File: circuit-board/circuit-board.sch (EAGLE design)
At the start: 42 parts, among them IC1 UA78M05DCY, Q1 BC547B, U1 MAX3232, U2 ATMEGA328P_TQFP, U3 ADUM1201BRZ, Y1 16MHz

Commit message: Delete V1 circuit board, replace with V2 working file
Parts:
- removed Y1: 16MHz, SparkFun-Clocks:CRYSTAL-16MHZPTH-HC49US
- added C1, C2, C21: 10uF, adafruit:CPOL-USE2.5-5
- added MIC-XFMR, SPK-XFMR: 42TL016, trafo-xicon:42TL016
- added OK1: 4N25SM, optocoupler:4N25SM
- added Q2: BC547B, transistor-npn:BC547B
- added R8: TRIMPOT, SparkFun:TRIMPOT
- added R9: (no value), rcl-2:R-TRIMM3296W
- added Y2: 16MHz, SparkFun-Clocks:CRYSTAL-GROUNDEDSMD-3.2X2.5
- R2: value 10k -> 120; device resistor:R-TRIMMT93YA -> SparkFun-Resistors:RESISTOR0603
- R6: value 0 -> 220; device SparkFun-Resistors:0OHM-0603-1/10W-5% -> SparkFun-Resistors:220OHM-0603-1/10W-1%
- renumbered 12V-IN to 12V-IN-GPS
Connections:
- new net N$2: C2.-, SPK-XFMR.6
- new net N$5: C2.+, Q2.B, R9.A
- new net N$6: C21.-, SPK-XFMR.1
- new net N$7: C5.-, MIC-XFMR.6
- new net N$9: OK1.A, R6.1
- new net RADIO-PTT-SENSE: OK1.COL, R4.2
- new net SPKAMP: C1.+, Q2.C, R2.1, R9.S
- net 12V: now also R2.2, R6.2
- net GND: now also MIC-XFMR.4, OK1.EMI, SPK-XFMR.3
- net GNDA: now also MIC-XFMR.3, Q2.E, SPK-XFMR.4, Y2.3
- net HANDSET-MIC: now also MIC-XFMR.1; no longer C5.-
- net HANDSET-PTT: now also OK1.C; no longer R4.1
- net HANDSET-SPK: now also C1.-; no longer R6.1
- net N$23: now also Y2.2; no longer Y1.2
- net N$24: now also Y2.1; no longer Y1.1
- net N$3: now also R8.CW; no longer R2.S
- net N$4: now also R8.WIPER; no longer R2.E
- net RADIO-MIC/PTT: now also R4.1; no longer R4.2
- net RADIO-SPK-OUT: now also C21.+; no longer R6.2
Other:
- moved on the sheet: C16, C17, C18, C19, C20, C5, C9, FB1, IC1, Q1, R3, R4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

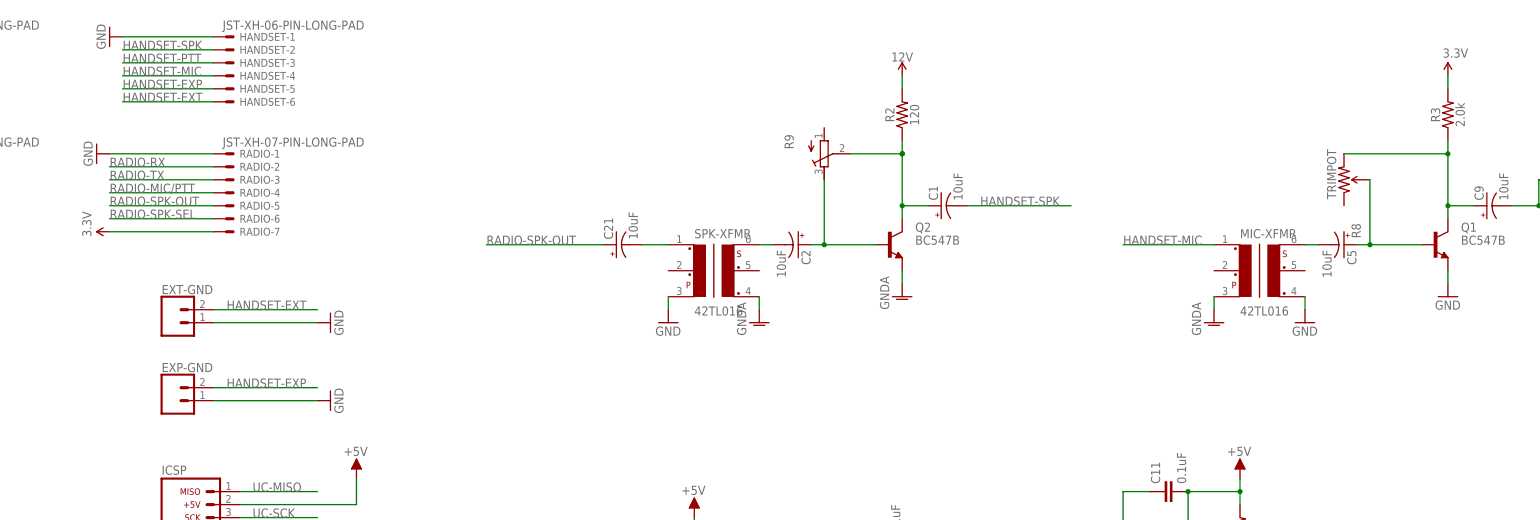
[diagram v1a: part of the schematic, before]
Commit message: Start new circuit board, fix some small circuit design issues
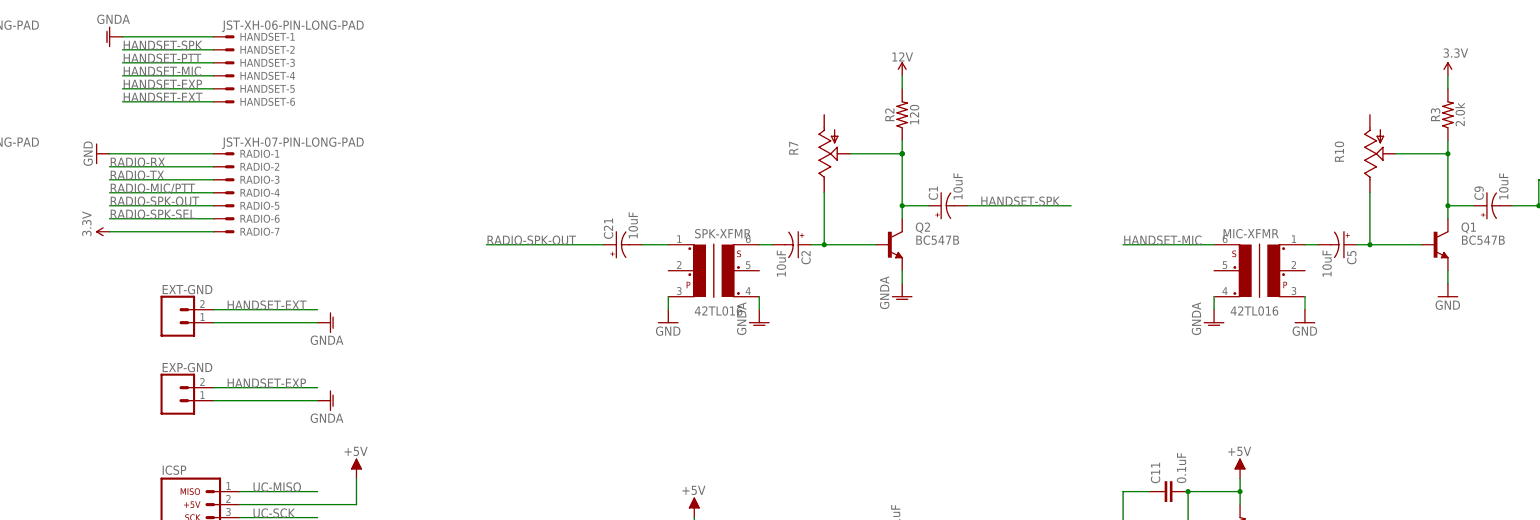
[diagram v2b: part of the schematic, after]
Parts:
- removed R8: TRIMPOT, SparkFun:TRIMPOT
- removed R9: (no value), rcl-2:R-TRIMM3296W
- added R10, R7: (no value), pot:TRIM_US-S64W
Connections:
- net GND: now also MIC-XFMR.3; no longer EXP-GND.1, EXT-GND.1, HANDSET-1.S, MIC-XFMR.4
- net GNDA: now also EXP-GND.1, EXT-GND.1, HANDSET-1.S, MIC-XFMR.4; no longer MIC-XFMR.3
- net HANDSET-MIC: now also MIC-XFMR.6; no longer MIC-XFMR.1
- net N$3: now also R10.S; no longer R8.CW
- net N$4: now also R10.E; no longer R8.WIPER
- net N$5: now also R7.E; no longer R9.A
- net N$7: now also MIC-XFMR.1; no longer MIC-XFMR.6
- net SPKAMP: now also R7.S; no longer R9.S

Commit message: Lay out circuit board, preliminary
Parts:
- renumbered 12V-IN-GPS to 12V-IN
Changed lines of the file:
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@@
 </classes>
 <parts>
-<part name="12V-IN-GPS" library="Rembrandt Electronics - JST XH Connectors v1-0" deviceset="JST-XH-02-PIN" device="-LONG-PAD"/>
+<part name="12V-IN" library="Rembrandt Electronics - JST XH Connectors v1-0" deviceset="JST-XH-02-PIN" device="-LONG-PAD"/>
 <part name="HANDSET" library="Rembrandt Electronics - JST XH Connectors v1-0" deviceset="JST-XH-06-PIN" device="-LONG-PAD"/>
 <part name="SUPPLY2" library="SparkFun-PowerSymbols" deviceset="12V" device=""/>
@@
 </plain>
 <instances>
-<instance part="12V-IN-GPS" gate="-2" x="-261.62" y="241.3"/>
-<instance part="12V-IN-GPS" gate="-1" x="-261.62" y="243.84"/>
+<instance part="12V-IN" gate="-2" x="-261.62" y="241.3"/>
+<instance part="12V-IN" gate="-1" x="-261.62" y="243.84"/>
 <instance part="HANDSET" gate="-1" x="-198.12" y="243.84"/>
 <instance part="HANDSET" gate="-2" x="-198.12" y="241.3"/>
@@
 </segment>
 <segment>
-<pinref part="12V-IN-GPS" gate="-1" pin="S"/>
+<pinref part="12V-IN" gate="-1" pin="S"/>
 <wire x1="-264.16" y1="243.84" x2="-269.24" y2="243.84" width="0.1524" layer="91"/>
 <pinref part="GND5" gate="1" pin="GNDA"/>
@@
 <segment>
 <pinref part="SUPPLY2" gate="G$1" pin="12V"/>
-<pinref part="12V-IN-GPS" gate="-2" pin="S"/>
+<pinref part="12V-IN" gate="-2" pin="S"/>
 <wire x1="-269.24" y1="241.3" x2="-264.16" y2="241.3" width="0.1524" layer="91"/>
 </segment>

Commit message: Add ground planes, routes to V2 board
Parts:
- R10, R7: value (none) -> 100k
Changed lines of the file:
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@@
 <grid distance="0.1" unitdist="inch" unit="inch" style="lines" multiple="1" display="no" altdistance="0.01" altunitdist="inch" altunit="inch"/>
 <layers>
-<layer number="1" name="Top" color="4" fill="1" visible="no" active="no"/>
-<layer number="16" name="Bottom" color="1" fill="1" visible="no" active="no"/>
-<layer number="17" name="Pads" color="2" fill="1" visible="no" active="no"/>
-<layer number="18" name="Vias" color="2" fill="1" visible="no" active="no"/>
-<layer number="19" name="Unrouted" color="6" fill="1" visible="no" active="no"/>
-<layer number="20" name="Dimension" color="15" fill="1" visible="no" active="no"/>
-<layer number="21" name="tPlace" color="7" fill="1" visible="no" active="no"/>
-<layer number="22" name="bPlace" color="7" fill="1" visible="no" active="no"/>
-<layer number="23" name="tOrigins" color="15" fill="1" visible="no" active="no"/>
-<layer number="24" name="bOrigins" color="15" fill="1" visible="no" active="no"/>
-<layer number="25" name="tNames" color="7" fill="1" visible="no" active="no"/>
-<layer number="26" name="bNames" color="7" fill="1" visible="no" active="no"/>
-<layer number="27" name="tValues" color="7" fill="1" visible="no" active="no"/>
-<layer number="28" name="bValues" color="7" fill="1" visible="no" active="no"/>
+<layer number="1" name="Top" color="4" fill="1" visible="yes" active="no"/>
+<layer number="16" name="Bottom" color="1" fill="1" visible="yes" active="no"/>
+<layer number="17" name="Pads" color="2" fill="1" visible="yes" active="no"/>
+<layer number="18" name="Vias" color="2" fill="1" visible="yes" active="no"/>
+<layer number="19" name="Unrouted" color="6" fill="1" visible="yes" active="no"/>
+<layer number="20" name="Dimension" color="24" fill="1" visible="yes" active="no"/>
+<layer number="21" name="tPlace" color="7" fill="1" visible="yes" active="no"/>
+<layer number="22" name="bPlace" color="7" fill="1" visible="yes" active="no"/>
+<layer number="23" name="tOrigins" color="15" fill="1" visible="yes" active="no"/>
+<layer number="24" name="bOrigins" color="15" fill="1" visible="yes" active="no"/>
+<layer number="25" name="tNames" color="7" fill="1" visible="yes" active="no"/>
+<layer number="26" name="bNames" color="7" fill="1" visible="yes" active="no"/>
+<layer number="27" name="tValues" color="7" fill="1" visible="yes" active="no"/>
+<layer number="28" name="bValues" color="7" fill="1" visible="yes" active="no"/>
 <layer number="29" name="tStop" color="7" fill="3" visible="no" active="no"/>
 <layer number="30" name="bStop" color="7" fill="6" visible="no" active="no"/>
@@
 <layer number="35" name="tGlue" color="7" fill="4" visible="no" active="no"/>
 <layer number="36" name="bGlue" color="7" fill="5" visible="no" active="no"/>
-<layer number="37" name="tTest" color="7" fill="1" visible="no" active="no"/>
-<layer number="38" name="bTest" color="7" fill="1" visible="no" active="no"/>
+<layer number="37" name="tTest" color="7" fill="1" visible="yes" active="no"/>
+<layer number="38" name="bTest" color="7" fill="1" visible="yes" active="no"/>
 <layer number="39" name="tKeepout" color="4" fill="11" visible="no" active="no"/>
 <layer number="40" name="bKeepout" color="1" fill="11" visible="no" active="no"/>
@@
 <layer number="44" name="Drills" color="7" fill="1" visible="no" active="no"/>
 <layer number="45" name="Holes" color="7" fill="1" visible="no" active="no"/>
-<layer number="46" name="Milling" color="3" fill="1" visible="no" active="no"/>
-<layer number="47" name="Measures" color="7" fill="1" visible="no" active="no"/>
-<layer number="48" name="Document" color="7" fill="1" visible="no" active="no"/>
-<layer number="49" name="Reference" color="7" fill="1" visible="no" active="no"/>
-<layer number="50" name="dxf" color="7" fill="1" visible="no" active="no"/>
-<layer number="51" name="tDocu" color="7" fill="1" visible="no" active="no"/>
-<layer number="52" name="bDocu" color="7" fill="1" visible="no" active="no"/>
-<layer number="53" name="tGND_GNDA" color="7" fill="9" visible="no" active="no"/>
-<layer number="54" name="bGND_GNDA" color="1" fill="9" visible="no" active="no"/>
-<layer number="56" name="wert" color="7" fill="1" visible="no" active="no"/>
-<layer number="57" name="tCAD" color="7" fill="1" visible="no" active="no"/>
-<layer number="59" name="tCarbon" color="7" fill="1" visible="no" active="no"/>
-<layer number="60" name="bCarbon" color="7" fill="1" visible="no" active="no"/>
+<layer number="46" name="Milling" color="3" fill="1" visible="yes" active="no"/>
+<layer number="47" name="Measures" color="7" fill="1" visible="yes" active="no"/>
+<layer number="48" name="Document" color="7" fill="1" visible="yes" active="no"/>
+<layer number="49" name="Reference" color="7" fill="1" visible="yes" active="no"/>
+<layer number="50" name="dxf" color="7" fill="1" visible="yes" active="no"/>
+<layer number="51" name="tDocu" color="7" fill="1" visible="yes" active="no"/>
+<layer number="52" name="bDocu" color="7" fill="1" visible="yes" active="no"/>
+<layer number="53" name="tGND_GNDA" color="7" fill="9" visible="yes" active="no"/>
+<layer number="54" name="bGND_GNDA" color="1" fill="9" visible="yes" active="no"/>
+<layer number="56" name="wert" color="7" fill="1" visible="yes" active="no"/>
+<layer number="57" name="tCAD" color="7" fill="1" visible="yes" active="no"/>
+<layer number="59" name="tCarbon" color="7" fill="1" visible="yes" active="no"/>
+<layer number="60" name="bCarbon" color="7" fill="1" visible="yes" active="no"/>
 <layer number="88" name="SimResults" color="9" fill="1" visible="yes" active="yes"/>
 <layer number="89" name="SimProbes" color="9" fill="1" visible="yes" active="yes"/>
@@
 <part name="GND24" library="supply1" deviceset="GNDA" device=""/>
 <part name="MIC-XFMR" library="trafo-xicon" library_urn="urn:adsk.eagle:library:393" deviceset="42T?*" device="L" package3d_urn="urn:adsk.eagle:package:28185/1" technology="016"/>
-<part name="R10" library="pot" library_urn="urn:adsk.eagle:library:331" deviceset="TRIM_US-" device="S64W" package3d_urn="urn:adsk.eagle:package:22708/1"/>
-<part name="R7" library="pot" library_urn="urn:adsk.eagle:library:331" deviceset="TRIM_US-" device="S64W" package3d_urn="urn:adsk.eagle:package:22708/1"/>
+<part name="R10" library="pot" library_urn="urn:adsk.eagle:library:331" deviceset="TRIM_US-" device="S64W" package3d_urn="urn:adsk.eagle:package:22708/1" value="100k"/>
+<part name="R7" library="pot" library_urn="urn:adsk.eagle:library:331" deviceset="TRIM_US-" device="S64W" package3d_urn="urn:adsk.eagle:package:22708/1" value="100k"/>
 <part name="GND10" library="supply1" deviceset="GNDA" device=""/>
 <part name="GND11" library="supply1" deviceset="GNDA" device=""/>

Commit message: Route V2 board manually, fix up silkscreen
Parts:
- U2: value ATMEGA328P_TQFP -> ATMEGA328P
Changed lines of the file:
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@@
 <grid distance="0.1" unitdist="inch" unit="inch" style="lines" multiple="1" display="no" altdistance="0.01" altunitdist="inch" altunit="inch"/>
 <layers>
-<layer number="1" name="Top" color="4" fill="1" visible="yes" active="no"/>
-<layer number="16" name="Bottom" color="1" fill="1" visible="yes" active="no"/>
-<layer number="17" name="Pads" color="2" fill="1" visible="yes" active="no"/>
-<layer number="18" name="Vias" color="2" fill="1" visible="yes" active="no"/>
-<layer number="19" name="Unrouted" color="6" fill="1" visible="yes" active="no"/>
-<layer number="20" name="Dimension" color="24" fill="1" visible="yes" active="no"/>
-<layer number="21" name="tPlace" color="7" fill="1" visible="yes" active="no"/>
-<layer number="22" name="bPlace" color="7" fill="1" visible="yes" active="no"/>
-<layer number="23" name="tOrigins" color="15" fill="1" visible="yes" active="no"/>
-<layer number="24" name="bOrigins" color="15" fill="1" visible="yes" active="no"/>
-<layer number="25" name="tNames" color="7" fill="1" visible="yes" active="no"/>
-<layer number="26" name="bNames" color="7" fill="1" visible="yes" active="no"/>
-<layer number="27" name="tValues" color="7" fill="1" visible="yes" active="no"/>
-<layer number="28" name="bValues" color="7" fill="1" visible="yes" active="no"/>
+<layer number="1" name="Top" color="4" fill="1" visible="no" active="no"/>
+<layer number="16" name="Bottom" color="1" fill="1" visible="no" active="no"/>
+<layer number="17" name="Pads" color="2" fill="1" visible="no" active="no"/>
+<layer number="18" name="Vias" color="2" fill="1" visible="no" active="no"/>
+<layer number="19" name="Unrouted" color="6" fill="1" visible="no" active="no"/>
+<layer number="20" name="Dimension" color="24" fill="1" visible="no" active="no"/>
+<layer number="21" name="tPlace" color="7" fill="1" visible="no" active="no"/>
+<layer number="22" name="bPlace" color="7" fill="1" visible="no" active="no"/>
+<layer number="23" name="tOrigins" color="15" fill="1" visible="no" active="no"/>
+<layer number="24" name="bOrigins" color="15" fill="1" visible="no" active="no"/>
+<layer number="25" name="tNames" color="7" fill="1" visible="no" active="no"/>
+<layer number="26" name="bNames" color="7" fill="1" visible="no" active="no"/>
+<layer number="27" name="tValues" color="7" fill="1" visible="no" active="no"/>
+<layer number="28" name="bValues" color="7" fill="1" visible="no" active="no"/>
 <layer number="29" name="tStop" color="7" fill="3" visible="no" active="no"/>
 <layer number="30" name="bStop" color="7" fill="6" visible="no" active="no"/>
@@
 <layer number="35" name="tGlue" color="7" fill="4" visible="no" active="no"/>
 <layer number="36" name="bGlue" color="7" fill="5" visible="no" active="no"/>
-<layer number="37" name="tTest" color="7" fill="1" visible="yes" active="no"/>
-<layer number="38" name="bTest" color="7" fill="1" visible="yes" active="no"/>
+<layer number="37" name="tTest" color="7" fill="1" visible="no" active="no"/>
+<layer number="38" name="bTest" color="7" fill="1" visible="no" active="no"/>
 <layer number="39" name="tKeepout" color="4" fill="11" visible="no" active="no"/>
 <layer number="40" name="bKeepout" color="1" fill="11" visible="no" active="no"/>
@@
 <layer number="44" name="Drills" color="7" fill="1" visible="no" active="no"/>
 <layer number="45" name="Holes" color="7" fill="1" visible="no" active="no"/>
-<layer number="46" name="Milling" color="3" fill="1" visible="yes" active="no"/>
-<layer number="47" name="Measures" color="7" fill="1" visible="yes" active="no"/>
-<layer number="48" name="Document" color="7" fill="1" visible="yes" active="no"/>
-<layer number="49" name="Reference" color="7" fill="1" visible="yes" active="no"/>
-<layer number="50" name="dxf" color="7" fill="1" visible="yes" active="no"/>
-<layer number="51" name="tDocu" color="7" fill="1" visible="yes" active="no"/>
-<layer number="52" name="bDocu" color="7" fill="1" visible="yes" active="no"/>
-<layer number="53" name="tGND_GNDA" color="7" fill="9" visible="yes" active="no"/>
-<layer number="54" name="bGND_GNDA" color="1" fill="9" visible="yes" active="no"/>
-<layer number="56" name="wert" color="7" fill="1" visible="yes" active="no"/>
-<layer number="57" name="tCAD" color="7" fill="1" visible="yes" active="no"/>
-<layer number="59" name="tCarbon" color="7" fill="1" visible="yes" active="no"/>
-<layer number="60" name="bCarbon" color="7" fill="1" visible="yes" active="no"/>
+<layer number="46" name="Milling" color="3" fill="1" visible="no" active="no"/>
+<layer number="47" name="Measures" color="7" fill="1" visible="no" active="no"/>
+<layer number="48" name="Document" color="7" fill="1" visible="no" active="no"/>
+<layer number="49" name="Reference" color="7" fill="1" visible="no" active="no"/>
+<layer number="50" name="dxf" color="7" fill="1" visible="no" active="no"/>
+<layer number="51" name="tDocu" color="7" fill="1" visible="no" active="no"/>
+<layer number="52" name="bDocu" color="7" fill="1" visible="no" active="no"/>
+<layer number="53" name="tGND_GNDA" color="7" fill="9" visible="no" active="no"/>
+<layer number="54" name="bGND_GNDA" color="1" fill="9" visible="no" active="no"/>
+<layer number="56" name="wert" color="7" fill="1" visible="no" active="no"/>
+<layer number="57" name="tCAD" color="7" fill="1" visible="no" active="no"/>
+<layer number="59" name="tCarbon" color="7" fill="1" visible="no" active="no"/>
+<layer number="60" name="bCarbon" color="7" fill="1" visible="no" active="no"/>
 <layer number="88" name="SimResults" color="9" fill="1" visible="yes" active="yes"/>
 <layer number="89" name="SimProbes" color="9" fill="1" visible="yes" active="yes"/>
@@
 <part name="GND14" library="supply1" deviceset="GNDA" device=""/>
 <part name="GND12" library="supply1" deviceset="GNDA" device=""/>
-<part name="U2" library="SparkFun-IC-Microcontroller" deviceset="ATMEGA328P_TQFP" device="" value="ATMEGA328P_TQFP"/>
+<part name="U2" library="SparkFun-IC-Microcontroller" deviceset="ATMEGA328P_TQFP" device="" value="ATMEGA328P"/>
 <part name="R5" library="SparkFun-Resistors" deviceset="10KOHM" device="-0603-1/10W-1%" value="10k"/>
 <part name="C11" library="SparkFun-Capacitors" deviceset="0.1UF" device="-0603-25V-5%" value="0.1uF"/>
